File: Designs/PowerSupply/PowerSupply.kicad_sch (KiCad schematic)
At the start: 18 parts, among them J1 Out, J2 In, SW1 SW_Push, T1 Transformer_1P_SS, U1 L7812, U2 L7912

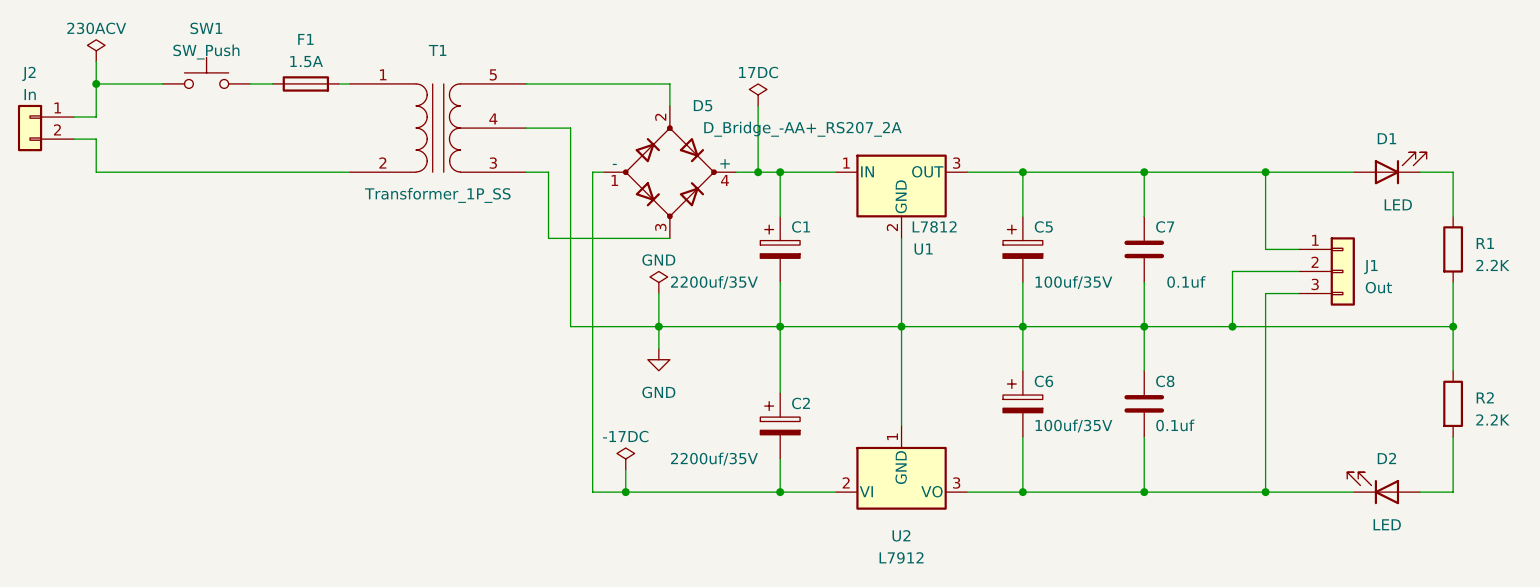
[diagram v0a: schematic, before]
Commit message: update powersupply design
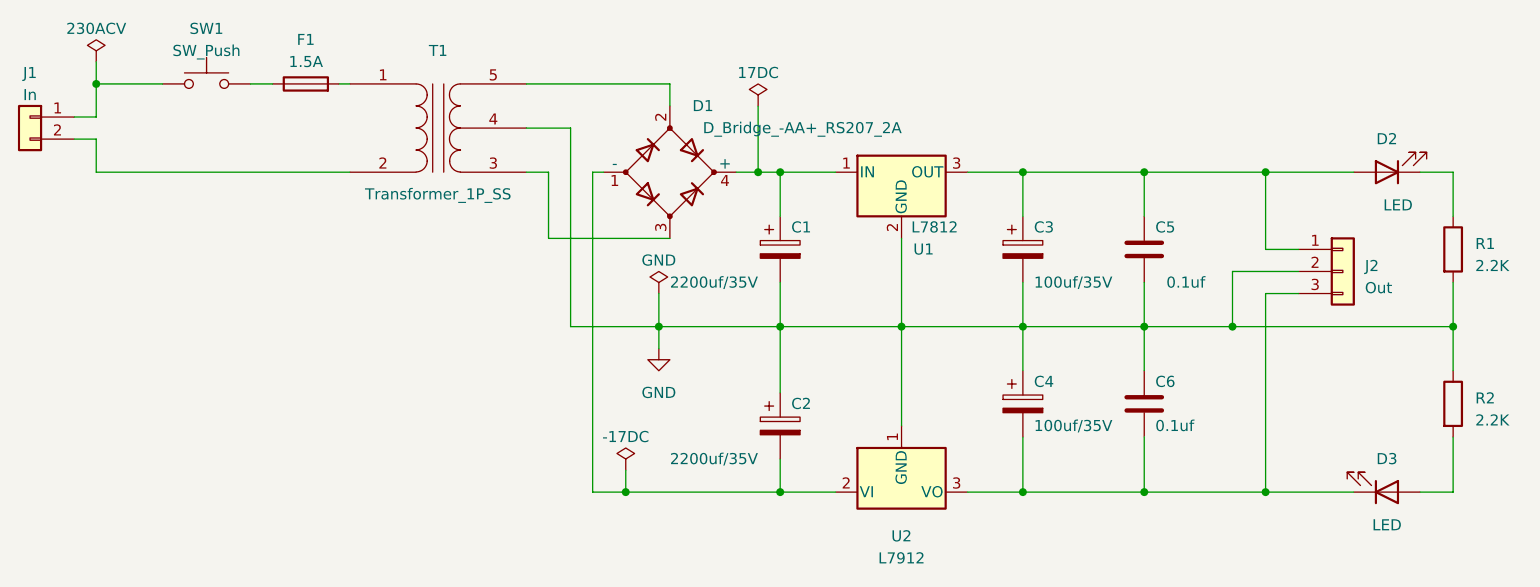
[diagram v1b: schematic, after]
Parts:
- renumbered C5 to C3, C6 to C4, C7 to C5, C8 to C6, D5 to D1, D1 to D2, D2 to D3, J2 to J1, J1 to J2
